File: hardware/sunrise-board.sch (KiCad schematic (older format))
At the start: 32 parts, among them J1 2.1mm Jack, J2 Header, J3 FTDI Basic, J4 Header, J5 Header, J6 Header, Q1 STP16NF06, Q2 STP16NF06, Q3 STP16NF06, SW1 Reset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

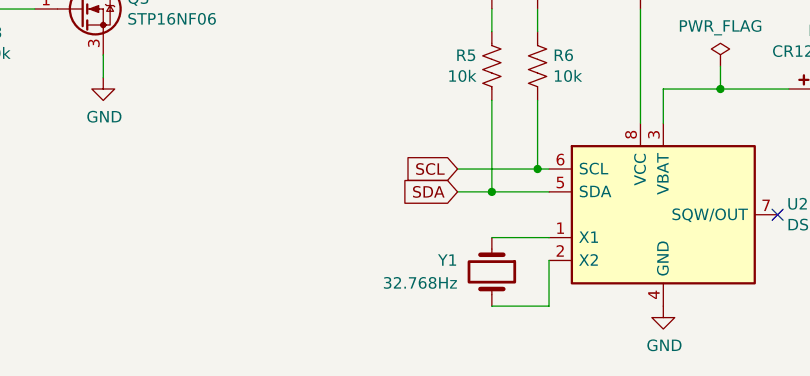
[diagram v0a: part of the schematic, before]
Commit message: fix crystal value
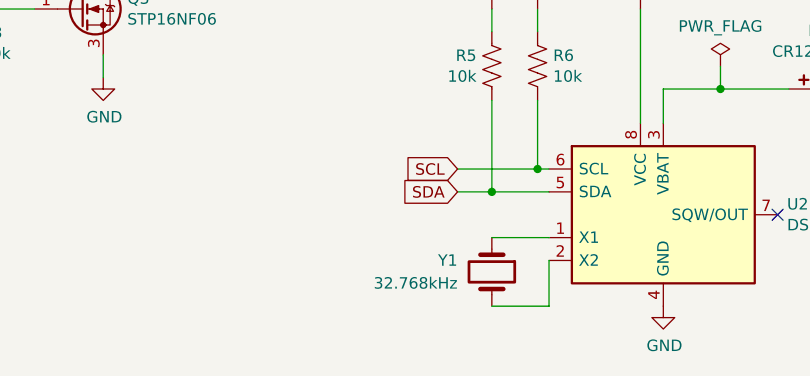
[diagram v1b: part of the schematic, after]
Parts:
- Y1: value 32.768Hz -> 32.768kHz
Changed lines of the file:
@@
 P 4200 6850
 F 0 "Y1" V 4150 6700 50  0000 R CNN
-F 1 "32.768Hz" V 4250 6700 50  0000 R CNN
+F 1 "32.768kHz" V 4250 6700 50  0000 R CNN
 F 2 "Crystal:Crystal_C26-LF_D2.1mm_L6.5mm_Horizontal_1EP_style2" H 4200 6850 50  0001 C CNN
 F 3 "https://www.iqdfrequencyproducts.com/products/pn/LFXTAL002997Bulk.pdf" H 4200 6850 50  0001 C CNN
